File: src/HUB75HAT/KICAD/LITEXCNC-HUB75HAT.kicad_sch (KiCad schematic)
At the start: 11 parts, among them J14 v7.0, J15 v8.0, J17 Conn_02x20_Odd_Even, U7 74HC04

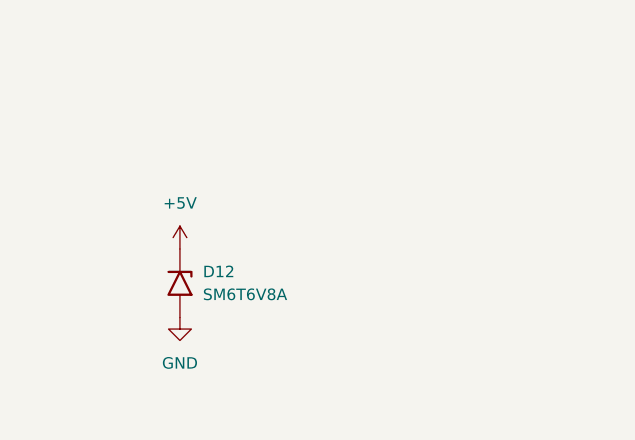
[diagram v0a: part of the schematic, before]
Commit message: Solved problem with J17 (GPIO header)
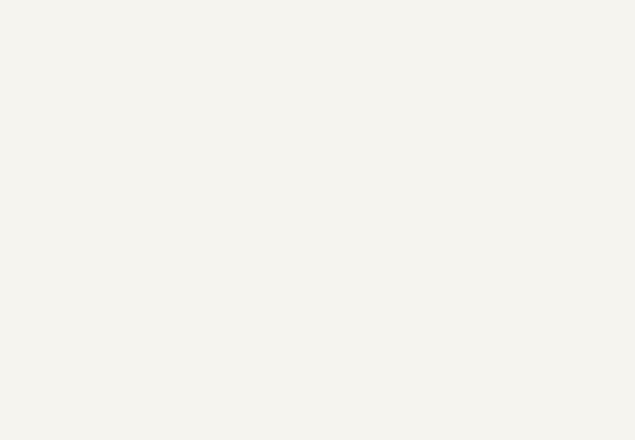
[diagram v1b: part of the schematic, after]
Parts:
- removed D12: SM6T6V8A, Diode_SMD:D_SMB, symbol Diode:SM6T6V8A
- J17: footprint Connector_PinHeader_2.54mm:PinHeader_2x20_P2.54mm_Vertical -> Connector_IDC:IDC-Header_2x20_P2.54mm_Vertical
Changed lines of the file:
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@@
-    )
-  )
-  (symbol (lib_id "power:GND") (at 26.67 184.15 0) (unit 1)
-    (in_bom yes) (on_board yes) (dnp no) (fields_autoplaced)
-    (property "Reference" "#PWR0106" (at 26.67 190.5 0)
-      (effects (font (size 1.27 1.27)) hide)
-    )
-    (property "Value" "GND" (at 26.67 189.23 0)
-      (effects (font (size 1.27 1.27)))
-    )
-    (property "Footprint" "" (at 26.67 184.15 0)
-      (effects (font (size 1.27 1.27)) hide)
-    )
-    (property "Datasheet" "" (at 26.67 184.15 0)
-      (effects (font (size 1.27 1.27)) hide)
-    )
-    (pin "1")
-    (instances
-      (project "LITEXCNC-HUB75HAT"
-        (path "/d03ad006-987f-4980-aa86-8f7e7030b027"
-          (reference "#PWR0106") (unit 1)
-        )
-      )
     )
   )
@@
         (path "/d03ad006-987f-4980-aa86-8f7e7030b027"
           (reference "#PWR0102") (unit 1)
-        )
-      )
-    )
-  )
-  (symbol (lib_id "power:+5V") (at 26.67 176.53 0) (unit 1)
-    (in_bom yes) (on_board yes) (dnp no) (fields_autoplaced)
-    (property "Reference" "#PWR0107" (at 26.67 180.34 0)
-      (effects (font (size 1.27 1.27)) hide)
-    )
-    (property "Value" "+5V" (at 26.67 171.45 0)
-      (effects (font (size 1.27 1.27)))
-    )
-    (property "Footprint" "" (at 26.67 176.53 0)
-      (effects (font (size 1.27 1.27)) hide)
-    )
-    (property "Datasheet" "" (at 26.67 176.53 0)
-      (effects (font (size 1.27 1.27)) hide)
-    )
-    (pin "1")
-    (instances
-      (project "LITEXCNC-HUB75HAT"
-        (path "/d03ad006-987f-4980-aa86-8f7e7030b027"
-          (reference "#PWR0107") (unit 1)
         )
       )
@@
     )
   )
-  (symbol (lib_id "Diode:SM6T6V8A") (at 26.67 180.34 270) (unit 1)
-    (in_bom yes) (on_board yes) (dnp no) (fields_autoplaced)
-    (property "Reference" "D12" (at 29.21 179.07 90)
-      (effects (font (size 1.27 1.27)) (justify left))
-    )
-    (property "Value" "SM6T6V8A" (at 29.21 181.61 90)
-      (effects (font (size 1.27 1.27)) (justify left))
-    )
-    (property "Footprint" "Diode_SMD:D_SMB" (at 21.59 180.34 0)
-      (effects (font (size 1.27 1.27)) hide)
-    )
-    (property "Datasheet" "https://www.st.com/resource/en/datasheet/sm6t.pdf" (at 26.67 179.07 0)
-      (effects (font (size 1.27 1.27)) hide)
-    )
-    (pin "1")
-    (pin "2")
-    (instances
-      (project "LITEXCNC-HUB75HAT"
-        (path "/d03ad006-987f-4980-aa86-8f7e7030b027"
-          (reference "D12") (unit 1)
-        )
-      )
-    )
-  )
   (symbol (lib_id "Connector_Generic:Conn_02x20_Odd_Even") (at 58.42 46.99 0) (unit 1)
     (in_bom yes) (on_board yes) (dnp no) (fields_autoplaced)
@@
       (effects (font (size 1.27 1.27)))
     )
-    (property "Footprint" "Connector_PinHeader_2.54mm:PinHeader_2x20_P2.54mm_Vertical" (at 58.42 46.99 0)
-      (effects (font (size 1.27 1.27)) hide)
-    )
+    (property "Footprint" "Connector_IDC:IDC-Header_2x20_P2.54mm_Vertical" (at 58.42 46.99 0)
+      (effects (font (size 1.27 1.27)) hide)
+    )
